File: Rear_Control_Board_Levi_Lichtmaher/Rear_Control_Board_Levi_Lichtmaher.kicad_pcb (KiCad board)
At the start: 2 copper layers, 297 x 210 mm, 85 parts, among them J1 430450200, J10 Molex Micro-Fit 4 Pin, J11 22035035, J12 22035035, J2 430450200, J3 430450200, J4 430450200, J5 430450200, J6 430450200, J7 430450200, J8 430450200, J9 22035035, Q2 PSMN1R8-40YLC_115, U11 MCP6286T-E/OT, U12 MCP6286T-E/OT, U2 ADS1118QDGSRQ1, U3 MCP2562-E/P, U4 UA78M05QDCYRG4Q1, U5 ASM330LHHTR, U6 MCP6286T-E/OT

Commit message: first draft PCB
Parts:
- added G***: LOGO, SMV_Logo:Shell, F.Cu at (148.0, 81.3)
- added Q1: PSMN1R8-40YLC_115, SMV_ICs:LFPAK56_SOT669_NEX-mosfet, F.Cu at (96.7, 77.1)
- added Q3: PSMN1R8-40YLC_115, SMV_ICs:LFPAK56_SOT669_NEX-mosfet, F.Cu at (96.7, 91.2)
- added Q4: PSMN1R8-40YLC_115, SMV_ICs:LFPAK56_SOT669_NEX-mosfet, F.Cu at (96.7, 100.2)
- added REF**: SEM_logo, SMV_Logo:SEM_logo, F.Cu at (103.0, 130.3)
- U3: footprint SMV_ICs:PDIP8_300MC_MCH -> SMV_ICs:SOIC127P600X175-8N
- moved H1 124.8 mm to (72.8, 45.0)
- moved H3 108.8 mm to (72.8, 140.0)
- moved TP43 107.0 mm to (90.6, 51.2)
- moved TP36 107.0 mm to (87.2, 68.0)
- moved J8 104.8 mm to (87.2, 100.2), turned to -90 degrees
- moved TP44 98.3 mm to (100.0, 49.7)
- moved J6 97.4 mm to (87.2, 109.1), turned to -90 degrees
- moved U4 96.2 mm to (100.0, 56.0)
- moved J4 94.0 mm to (87.2, 117.6), turned to -90 degrees
- moved J7 91.5 mm to (87.2, 91.1), turned to -90 degrees
- moved Q2 91.1 mm to (96.7, 113.2), turned to 90 degrees
- moved TP7 89.2 mm to (95.8, 59.1)
- moved J2 84.4 mm to (191.6, 47.7), turned to 90 degrees
- moved R11 83.9 mm to (103.0, 115.7)
- moved R3 82.4 mm to (98.2, 109.2), turned to 180 degrees
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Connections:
- U2 pad 4: /Pressure -> /Torque_P_ADC
- U2 pad 6: /Torque_P_ADC -> /Pressure
- U7 pad CN10_11: (no net) -> unconnected-(U7-PA5-PadCN10_11)
- U7 pad CN10_13: (no net) -> unconnected-(U7-PA6-PadCN10_13)
- U7 pad CN10_15: (no net) -> unconnected-(U7-PA7-PadCN10_15)
- U7 pad CN10_17: (no net) -> unconnected-(U7-PB6-PadCN10_17)
- U7 pad CN10_19: (no net) -> unconnected-(U7-PC7-PadCN10_19)
- U7 pad CN10_21: (no net) -> unconnected-(U7-PA9-PadCN10_21)
- U7 pad CN10_23: (no net) -> unconnected-(U7-PA8-PadCN10_23)
- U7 pad CN10_25: (no net) -> unconnected-(U7-PB10-PadCN10_25)
- U7 pad CN10_27: (no net) -> Net-(U7-PB4)
- U7 pad CN10_28: (no net) -> Net-(U7-PB14)
- U7 pad CN10_29: (no net) -> unconnected-(U7-PB5-PadCN10_29)
- U7 pad CN10_3: (no net) -> /RX
- U7 pad CN10_31: (no net) -> unconnected-(U7-PB3-PadCN10_31)
- U7 pad CN10_33: (no net) -> unconnected-(U7-PA10-PadCN10_33)
- U7 pad CN10_35: (no net) -> unconnected-(U7-PA2-PadCN10_35)
- U7 pad CN10_37: (no net) -> unconnected-(U7-PA3-PadCN10_37)
- U7 pad CN10_5: (no net) -> /TX
- U7 pad CN10_7: (no net) -> +3V3
- U7 pad CN10_9: (no net) -> GND
- U7 pad CN5_1: unconnected-(U7-PA9-PadCN5_1) -> (no net)
- U7 pad CN5_10: /RX -> (no net)
- U7 pad CN5_2: unconnected-(U7-PC7-PadCN5_2) -> (no net)
- U7 pad CN5_3: unconnected-(U7-PB6-PadCN5_3) -> (no net)
- U7 pad CN5_4: unconnected-(U7-PA7-PadCN5_4) -> (no net)
- U7 pad CN5_5: unconnected-(U7-PA6-PadCN5_5) -> (no net)
- U7 pad CN5_6: unconnected-(U7-PA5-PadCN5_6) -> (no net)
- U7 pad CN5_7: GND -> (no net)
- U7 pad CN5_8: +3V3 -> (no net)
- U7 pad CN5_9: /TX -> (no net)
- U7 pad CN6_2: unconnected-(U7-IOREF-PadCN6_2) -> (no net)
- U7 pad CN6_3: unconnected-(U7-RESET-PadCN6_3) -> (no net)
- U7 pad CN6_4: +3V3 -> (no net)
- U7 pad CN6_5: unconnected-(U7-+5V-PadCN6_5) -> (no net)
- U7 pad CN6_6: GND -> (no net)
- U7 pad CN6_7: GND -> (no net)
- U7 pad CN6_8: unconnected-(U7-VIN-PadCN6_8) -> (no net)
- U7 pad CN7_12: (no net) -> unconnected-(U7-IOREF-PadCN7_12)
- U7 pad CN7_13: unconnected-(U7-PA13-PadCN7_13) -> /Tail Lights
- U7 pad CN7_14: (no net) -> unconnected-(U7-RESET-PadCN7_14)
- U7 pad CN7_15: unconnected-(U7-PA14-PadCN7_15) -> /Turn Signal Light 1
- U7 pad CN7_16: (no net) -> +3V3
- U7 pad CN7_18: (no net) -> unconnected-(U7-+5V-PadCN7_18)
- U7 pad CN7_20: (no net) -> GND
- U7 pad CN7_21: unconnected-(U7-PB7-PadCN7_21) -> /Turn Signal Light 2
- U7 pad CN7_22: (no net) -> GND
- U7 pad CN7_24: (no net) -> unconnected-(U7-VIN-PadCN7_24)
- U7 pad CN7_28: (no net) -> unconnected-(U7-PA0-PadCN7_28)
- U7 pad CN7_30: (no net) -> unconnected-(U7-PA1-PadCN7_30)
- U7 pad CN7_31: unconnected-(U7-PH1-PadCN7_31) -> /Brake Lights
- U7 pad CN7_32: (no net) -> unconnected-(U7-PA4-PadCN7_32)
- U7 pad CN7_34: (no net) -> unconnected-(U7-PB0-PadCN7_34)
- U7 pad CN7_36: (no net) -> unconnected-(U7-PC1-PadCN7_36)
- U7 pad CN7_38: (no net) -> unconnected-(U7-PC0-PadCN7_38)
- U7 pad CN8_1: unconnected-(U7-PA0-PadCN8_1) -> (no net)
- U7 pad CN8_2: unconnected-(U7-PA1-PadCN8_2) -> (no net)
- U7 pad CN8_3: unconnected-(U7-PA4-PadCN8_3) -> (no net)
- U7 pad CN8_4: unconnected-(U7-PB0-PadCN8_4) -> (no net)
- U7 pad CN8_5: unconnected-(U7-PC1-PadCN8_5) -> (no net)
- U7 pad CN8_6: unconnected-(U7-PC0-PadCN8_6) -> (no net)
- U7 pad CN9_1: unconnected-(U7-PA3-PadCN9_1) -> (no net)
- U7 pad CN9_2: unconnected-(U7-PA2-PadCN9_2) -> (no net)
- U7 pad CN9_3: unconnected-(U7-PA10-PadCN9_3) -> (no net)
- U7 pad CN9_4: /Turn Signal Light 1 -> (no net)
- U7 pad CN9_5: /Tail Lights -> (no net)
- U7 pad CN9_6: Net-(U7-PB4) -> (no net)
- U7 pad CN9_7: /Turn Signal Light 2 -> (no net)
- U7 pad CN9_8: /Brake Lights -> (no net)
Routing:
- net +3V3: track 0.00 -> 327.6 mm, vias 0 -> 2
- net +12V: track 0.00 -> 275.3 mm
- net +5V: track 0.00 -> 139.7 mm
- net GND: track 0.00 -> 52.9 mm, vias 0 -> 47
- net Net-(U7-PB12): track 0.00 -> 50.7 mm
- net /SCK: track 0.00 -> 39.4 mm, vias 0 -> 2
- net /MOSI: track 0.00 -> 32.1 mm
- net /CAN_N: track 0.00 -> 27.7 mm
- net /CAN_P: track 0.00 -> 27.7 mm
- net /Pressure: track 0.00 -> 25.7 mm
- net /Torque_P_ADC: track 0.00 -> 25.1 mm
- net /TX: track 0.00 -> 20.4 mm
- net Net-(U7-PB4): track 0.00 -> 16.7 mm
- net /Tail Lights: track 0.00 -> 14.6 mm
- net Net-(Q2-Drain): track 0.00 -> 13.9 mm
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- added copper zone on B.Cu, net GND
- added copper zone on F.Cu, net GND
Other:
- board size 297 x 210 mm -> 149.2 x 106.5 mm
- board text added: "(insures victory)"
- board text added: "Brake Lights"
- board text added: "C14"
- board text added: "CAN"
- board text added: "IDK what to do with this and IDK where to get 2.5V"
- board text added: "Power"
- board text added: "Pressure"
- board text added: "Rear Control Board 12/27/2025 University of California, Los Angeles By Levi Lichtmaher"
- board text added: "Secret Shell"
- board text added: "Tail Lights"
- board text added: "This feels like empty space can i put cool images here or smth"
- board text added: "Torque"
- board text added: "Turn Signal #1"
- board text added: "Turn Signal #2"

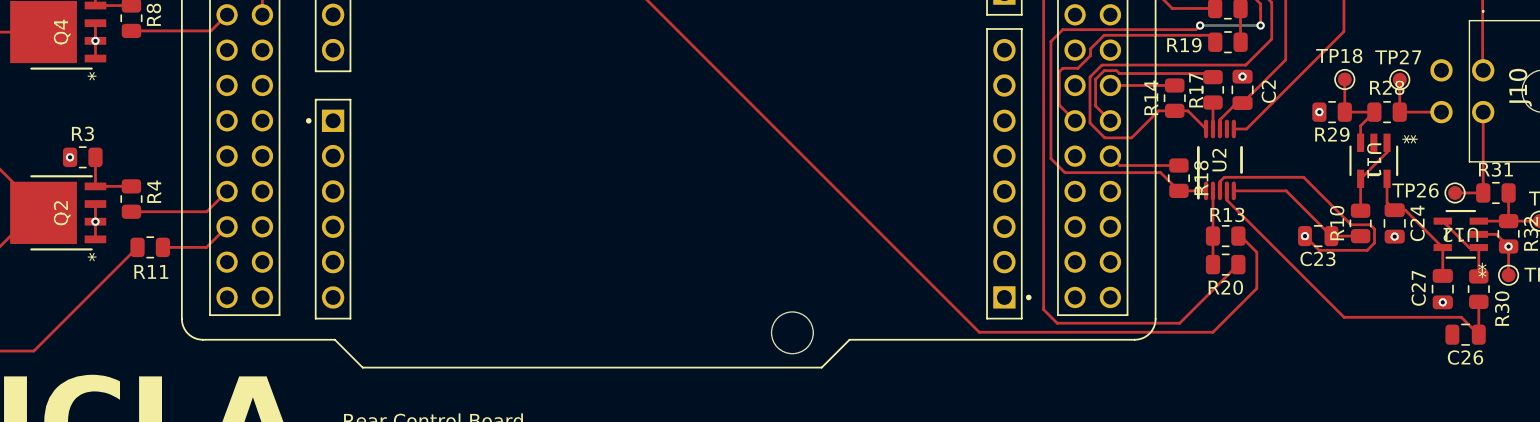
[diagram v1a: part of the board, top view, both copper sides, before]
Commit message: added LED for testing
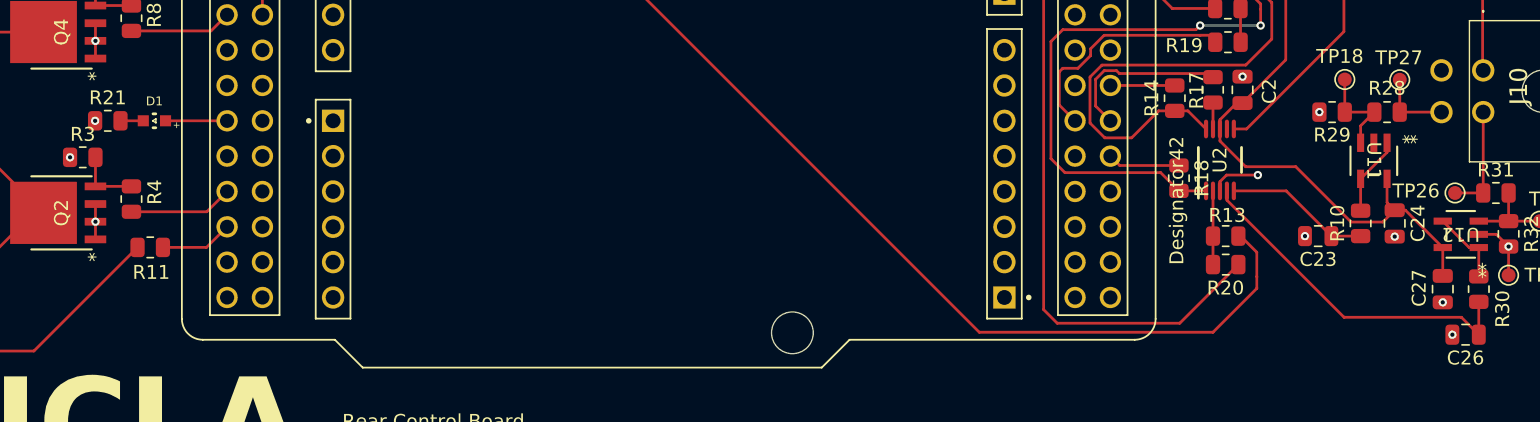
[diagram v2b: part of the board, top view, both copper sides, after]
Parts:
- added D1: LED, SMV_Passives:WL-SMCW_0603(diode), F.Cu at (103.3, 106.5)
- added R21: 150, Resistor_SMD:R_0805_2012Metric, F.Cu at (100.0, 106.5)
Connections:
- U7 pad CN7_27: unconnected-(U7-PC15-PadCN7_27) -> Net-(D1-A)
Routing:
- net GND: track 52.9 -> 36.4 mm, vias 47 -> 50
- net +3V3: track 327.6 -> 343.7 mm
- net Net-(D1-A): track 0.00 -> 4.42 mm
- net Net-(D1-K): track 0.00 -> 1.64 mm

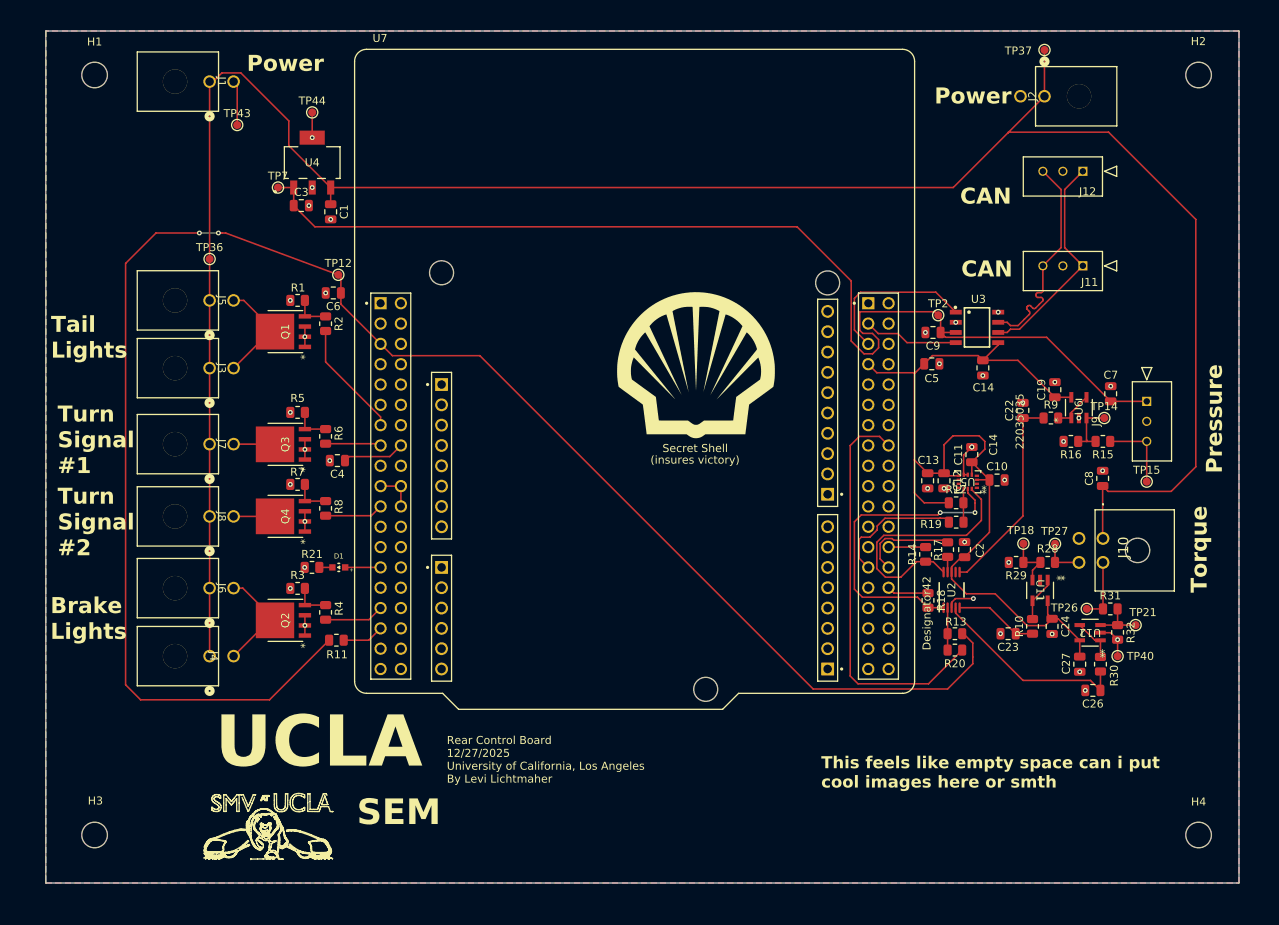
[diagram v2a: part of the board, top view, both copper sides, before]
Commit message: fixed vias, made power traces wider
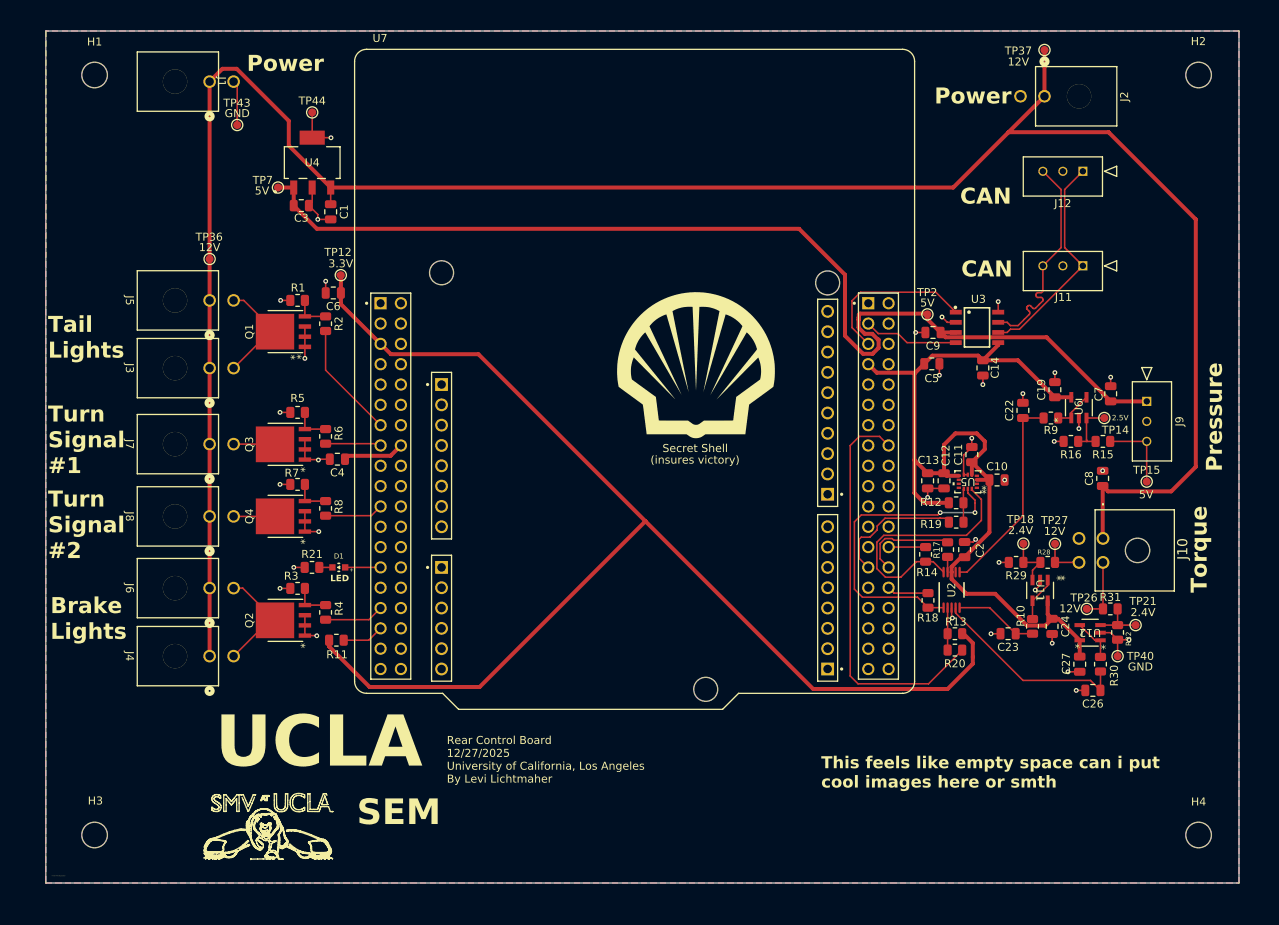
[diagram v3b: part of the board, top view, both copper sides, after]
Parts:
- moved 5V 1.35 mm to (176.9, 74.9)
- moved 3.3V 0.32 mm to (103.6, 70.0)
- moved C4 0.17 mm to (103.2, 93.0)
- renumbered TP27 to 12V, TP36 to 12V, TP18 to 2.4V, TP21 to 2.4V, TP12 to 3.3V, TP2 to 5V, TP43 to GND
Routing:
- net +3V3: track 343.7 -> 283.9 mm, vias 2 -> 0
- net GND: track 36.4 -> 81.4 mm, vias 50 -> 38
- net +5V: track 139.7 -> 138.7 mm
- net +12V: track 275.3 -> 276.1 mm
- net /Tail Lights: track 14.6 -> 15.3 mm
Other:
- board text added: "12V"
- board text added: "2.5V"
- board text added: "430450200"
- board text added: "5V"
- board text added: "GND"
- board text added: "I wonder if this will get printed"
- board text added: "LED"
- board text added: "TP12"
- board text added: "TP18"
- board text added: "TP2"
- board text added: "TP21"
- board text added: "TP27"
- board text added: "TP36"
- board text added: "TP43"

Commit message: updated PCB
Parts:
- renumbered U2 to ADC
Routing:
- net +5V: track 138.7 -> 135.4 mm
- net GND: vias 38 -> 37
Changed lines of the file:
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@@
 		(at 179.95 109.3625 90)
 		(tags "ADS1115IDGSR ")
-		(property "Reference" "U2"
-			(at 0 0 90)
+		(property "Reference" "ADC"
+			(at 1.0375 2.525 90)
 			(unlocked yes)
 			(layer "F.SilkS")
 			(effects
 				(font
-					(size 1 1)
+					(size 0.9 0.9)
 					(thickness 0.15)
 				)
@@
 	)
 	(via
-		(at 172.075 111.63)
-		(size 0.6)
-		(drill 0.3)
-		(layers "F.Cu" "B.Cu")
-		(net 2)
-	)
-	(via
 		(at 198.832501 94.475)
 		(size 0.6)
@@
 	)
 	(segment
-		(start 168.325 75.3)
-		(end 168.351 75.274)
-		(width 0.5)
-		(layer "F.Cu")
-		(net 8)
-	)
-	(segment
-		(start 170.75 78.075)
-		(end 170.025 77.35)
+		(start 160.8849 64.225)
+		(end 166.625 69.9651)
 		(width 0.5)
 		(layer "F.Cu")
@@
 	)
 	(segment
-		(start 97.7136 61.325)
-		(end 100.6136 64.225)
+		(start 166.625 77.6)
+		(end 168.875 79.85)
 		(width 0.5)
 		(layer "F.Cu")
@@
 	)
 	(segment
-		(start 178.575 77.185)
-		(end 179.176 77.786)
+		(start 176.788636 79.85)
+		(end 177.260636 79.378)
 		(width 0.5)
 		(layer "F.Cu")
@@
 	)
 	(segment
-		(start 168.875 79.85)
-		(end 170.075 79.85)
+		(start 166.625 69.9651)
+		(end 166.625 77.6)
 		(width 0.5)
 		(layer "F.Cu")
@@
 	)
 	(segment
-		(start 168.351 74.974)
-		(end 168.5 74.825)
+		(start 182.1 79.378)
+		(end 182.1 77.7)
 		(width 0.5)
 		(layer "F.Cu")
@@
 	)
 	(segment
-		(start 168.5 74.825)
-		(end 176.825 74.825)
-		(width 0.5)
-		(layer "F.Cu")
-		(net 8)
-	)
-	(segment
 		(start 97.7136 59.06785)
 		(end 97.7136 61.325)
@@
 	)
 	(segment
-		(start 170.825 79.1)
-		(end 170.825 78.075)
-		(width 0.5)
-		(layer "F.Cu")
-		(net 8)
-	)
-	(segment
 		(start 97.71785 59.34575)
 		(end 97.7136 59.35)
@@
 	)
 	(segment
-		(start 168.351 75.274)
-		(end 168.351 74.974)
-		(width 0.5)
-		(layer "F.Cu")
-		(net 8)
-	)
-	(segment
-		(start 168.319 75.566316)
-		(end 168.325 75.560316)
-		(width 0.5)
+		(start 191.764301 77.85)
+		(end 182.25 77.85)
+		(width 0.2)
 		(layer "F.Cu")
 		(net 8)
 	)
 	(segment
-		(start 168.325 75.560316)
-		(end 168.325 75.3)
-		(width 0.5)
+		(start 191.828301 77.786)
+		(end 191.764301 77.85)
+		(width 0.2)
 		(layer "F.Cu")
 		(net 8)
 	)
 	(segment
-		(start 170.075 79.85)
-		(end 170.825 79.1)
-		(width 0.5)
-		(layer "F.Cu")
-		(net 8)
-	)
-	(segment
-		(start 166.625 69.9651)
-		(end 166.625 77.6)
+		(start 177.260636 79.378)
+		(end 182.1 79.378)
 		(width 0.5)
 		(layer "F.Cu")
@@
 	)
 	(segment
-		(start 191.828301 77.786)
-		(end 199.8375 85.795199)
+		(start 181.585 77.185)
+		(end 180.475 77.185)
 		(width 0.5)
 		(layer "F.Cu")
@@
 	)
 	(segment
-		(start 168.319 76.573684)
-		(end 168.319 75.566316)
-		(width 0.5)
+		(start 97.7136 59.06785)
+		(end 97.71785 59.0721)
+		(width 0.2)
 		(layer "F.Cu")
 		(net 8)
 	)
 	(segment
-		(start 170.825 78.075)
-		(end 170.75 78.075)
+		(start 97.7136 61.325)
+		(end 100.6136 64.225)
 		(width 0.5)
 		(layer "F.Cu")
@@
 	)
 	(segment
-		(start 97.7136 59.06785)
-		(end 97.71785 59.0721)
-		(width 0.2)
+		(start 182.1 77.7)
+		(end 181.585 77.185)
+		(width 0.5)
 		(layer "F.Cu")
 		(net 8)
@@
 	)
 	(segment
-		(start 170.025 77.35)
-		(end 169.095316 77.35)
-		(width 0.5)
-		(layer "F.Cu")
-		(net 8)
-	)
-	(segment
 		(start 178.575 77.185)
 		(end 180.475 77.185)
@@
 	)
 	(segment
-		(start 97.71785 59.0721)
-		(end 97.71785 59.34575)
+		(start 182.25 77.85)
+		(end 182.1 77.7)
 		(width 0.2)
 		(layer "F.Cu")
@@
 	)
 	(segment
-		(start 169.095316 77.35)
-		(end 168.319 76.573684)
-		(width 0.5)
-		(layer "F.Cu")
-		(net 8)
-	)
-	(segment
-		(start 160.8849 64.225)
-		(end 166.625 69.9651)
+		(start 191.828301 77.786)
+		(end 199.8375 85.795199)
 		(width 0.5)
 		(layer "F.Cu")
@@
 	)
 	(segment
-		(start 166.625 77.6)
-		(end 168.875 79.85)
-		(width 0.5)
+		(start 97.71785 59.0721)
+		(end 97.71785 59.34575)
+		(width 0.2)
 		(layer "F.Cu")
 		(net 8)
 	)
 	(segment
-		(start 179.176 77.786)
-		(end 191.828301 77.786)
+		(start 168.875 79.85)
+		(end 176.788636 79.85)
 		(width 0.5)
 		(layer "F.Cu")
@@
 	)
 	(segment
+		(start 189.45134 113.9)
+		(end 191.587501 113.9)
+		(width 0.5)
+		(layer "F.Cu")
+		(net 17)
+	)
+	(segment
 		(start 183.1106 95.599748)
 		(end 184.655426 95.599748)
@@
 	)
 	(segment
-		(start 189.37734 113.826)
-		(end 191.661501 113.826)
-		(width 0.5)
-		(layer "F.Cu")
-		(net 17)
-	)
-	(segment
 		(start 177.551 80.079)
 		(end 183.274 80.079)
@@
 	)
 	(segment
-		(start 185.40034 109.849)
-		(end 189.37734 113.826)
+		(start 184.1 91.780174)
+		(end 182.480426 93.399748)
 		(width 0.5)
 		(layer "F.Cu")
@@
 	)
 	(segment
-		(start 184.1 91.780174)
-		(end 182.480426 93.399748)
+		(start 108.575 78.61)
+		(end 103.612501 73.647501)
 		(width 0.5)
 		(layer "F.Cu")
@@
 	)
 	(segment
-		(start 108.575 78.61)
-		(end 103.612501 73.647501)
+		(start 185.40034 109.849)
+		(end 189.45134 113.9)
 		(width 0.5)
 		(layer "F.Cu")
@@
 	)
 	(segment
-		(start 181.799 109.849)
-		(end 185.40034 109.849)
-		(width 0.5)
-		(layer "F.Cu")
-		(net 17)
-	)
-	(segment
 		(start 176.525 81.105)
 		(end 175.414 82.216)
@@
 	)
 	(segment
-		(start 179.95 108)
-		(end 181.799 109.849)
-		(width 0.5)
-		(layer "F.Cu")
-		(net 17)
-	)
-	(segment
 		(start 111.115 91.31)
 		(end 109.825 92.6)
@@
 	)
 	(segment
-		(start 179.95 107.137498)
-		(end 179.95 108)
-		(width 0.5)
-		(layer "F.Cu")
-		(net 17)
-	)
-	(segment
 		(start 184.680426 102.169574)
 		(end 181.575 105.275)
@@
 	)
 	(segment
-		(start 191.661501 113.826)
-		(end 192.512501 112.975)
+		(start 104.55 92.6)
+		(end 104.125 93.025)
 		(width 0.5)
 		(layer "F.Cu")
@@
 	)
 	(segment
-		(start 104.55 92.6)
-		(end 104.125 93.025)
+		(start 191.587501 113.9)
+		(end 192.512501 112.975)
 		(width 0.5)
 		(layer "F.Cu")
@@
 	)
 	(segment
+		(start 179.95 108)
+		(end 181.799 109.849)
+		(width 0.5)
+		(layer "F.Cu")
+		(net 17)
+	)
+	(segment
 		(start 175.414 82.216)
 		(end 175.3 82.216)
@@
 	)
 	(segment
+		(start 181.799 109.849)
+		(end 185.40034 109.849)
+		(width 0.5)
+		(layer "F.Cu")
+		(net 17)
+	)
+	(segment
 		(start 184.655426 95.599748)
 		(end 184.680426 95.624748)
@@
 		(width 0.5)
 		(layer "F.Cu")
+		(net 17)
+	)
+	(segment
+		(start 179.95 107.137498)
+		(end 179.95 108)
+		(width 0.5)
+		(layer "F.Cu")
